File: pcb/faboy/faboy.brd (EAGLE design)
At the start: 85.1 x 54 mm, 58 parts, among them U1 MAX1595UMAX, U2 MCP73831, Y1 16MHZ

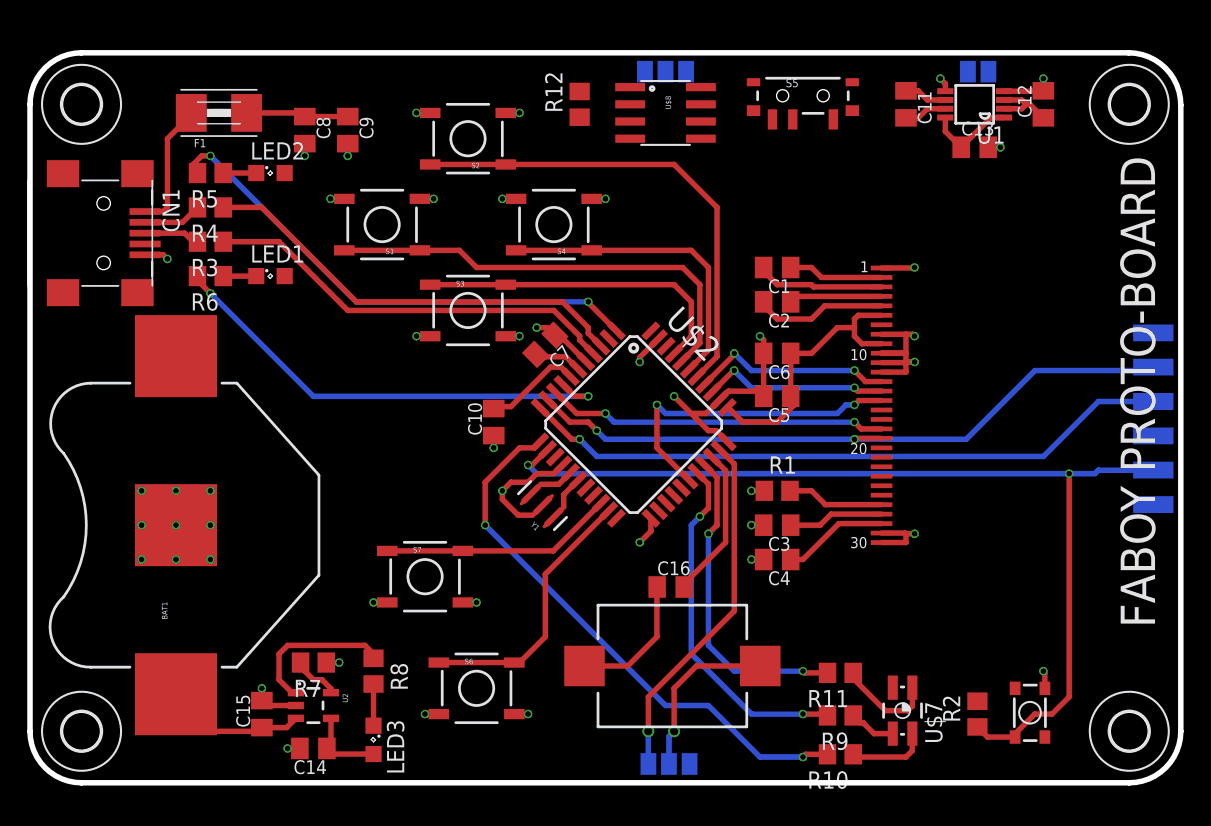
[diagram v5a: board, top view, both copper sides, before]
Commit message: pcb > end of routing
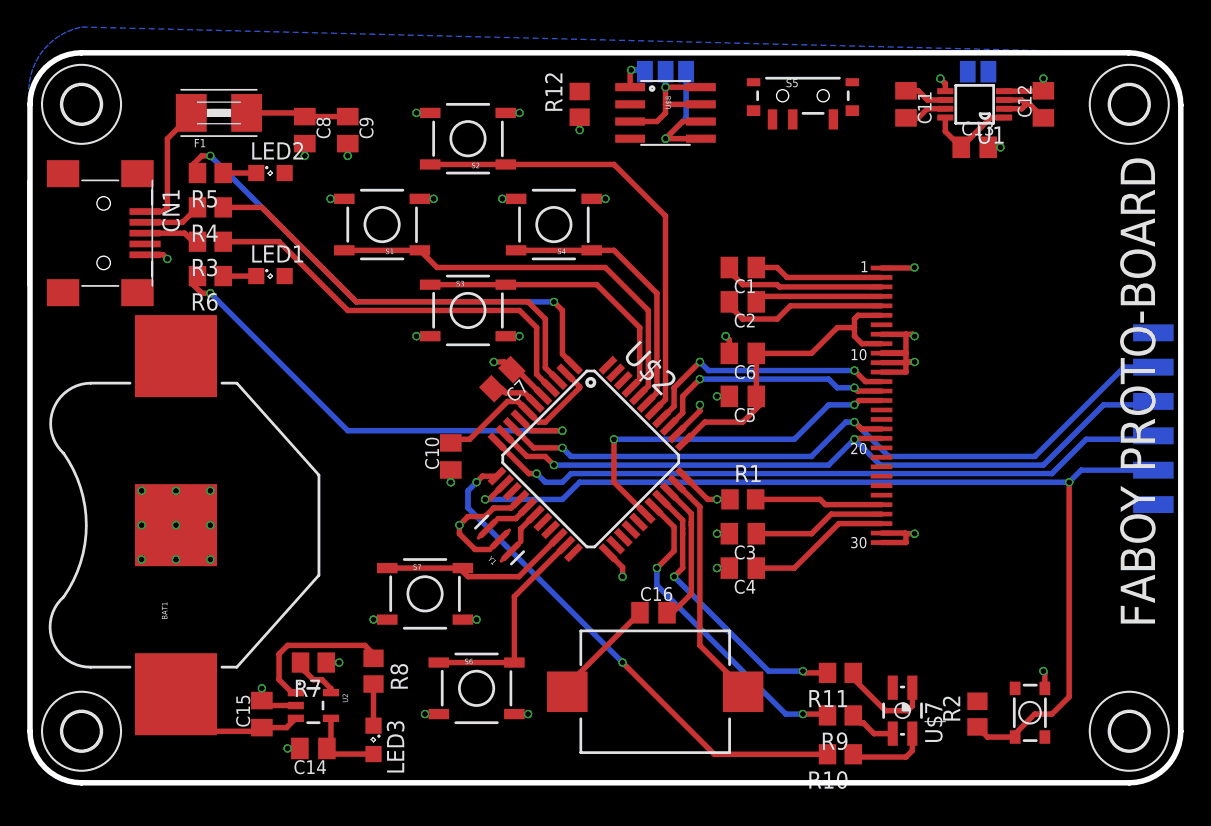
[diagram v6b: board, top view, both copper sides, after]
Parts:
- removed SJ2: (no value), jumper:SJ_2
- SJ1: value (none) -> direct power
- SJ3: value (none) -> direct path
- U$5: value (none) -> gnd
- moved C10 4.07 mm to (31.1, 24.1)
- moved C7 4.07 mm to (34.9, 29.8)
- moved Y1 4.07 mm to (34.7, 18.0)
- moved U$2 4.07 mm to (41.5, 23.9)
- moved C3 2.62 mm to (52.7, 18.4)
- moved C4 2.62 mm to (52.7, 15.9)
- moved R1 2.62 mm to (52.7, 21.0)
- moved C1 2.54 mm to (52.7, 38.1)
- moved C2 2.54 mm to (52.7, 35.6)
- moved C5 2.54 mm to (52.7, 28.6)
- moved C6 2.54 mm to (52.7, 31.8)
- moved C16 2.29 mm to (46.1, 12.6)
- moved SG1 2.29 mm to (46.2, 6.73)
- moved S7 1.27 mm to (29.2, 14.0)
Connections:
- removed net N$27: SJ2.3, U$2.32
- net GND: no longer SJ2.1
- net MISO: now also J2.3; no longer J2.4
- net MOSI: now also J2.4; no longer J2.5
- net N$26: now also U$2.32; no longer SJ2.2
- net SCLK: now also J2.5; no longer J2.3
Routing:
- net SCLK: track 25.3 -> 55.4 mm
- net N$27: track 26.3 -> 0.00 mm, vias 1 -> 0
- net VBAT: track 10.5 -> 21.9 mm, vias 0 -> 1
- net N$28: track 0.00 -> 11.2 mm, vias 0 -> 1
- net GND: track 87.0 -> 78.1 mm, vias 45 -> 46
- net UVCC: track 16.8 -> 23.5 mm
- net N$26: track 12.8 -> 17.4 mm, vias 1 -> 0
- net CS: track 15.0 -> 19.4 mm
- net OLED_RST: track 13.8 -> 18.2 mm
- net B: track 19.9 -> 15.9 mm
- net MOSI: track 50.5 -> 54.5 mm
- net DC: track 23.8 -> 27.5 mm
- net VCC: track 27.7 -> 31.1 mm
- net RST: track 73.5 -> 76.6 mm
- net A: track 17.3 -> 14.3 mm
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- added copper zone on layer 16, net GND

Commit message: pcb > final with silk
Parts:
- moved R12 1.27 mm to (40.6, 48.9)
- turned S2 to 0 degrees
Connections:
- removed net UVCC: C10.2, CN1.VBUS, F1.1, U$2.2, U$2.7
- new net VBUS: CN1.VBUS, F1.1
- net VIN: now also C10.2, U$2.2, U$2.7
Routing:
- net VCC: track 31.1 -> 85.9 mm, vias 0 -> 4
- net VIN: track 15.9 -> 40.5 mm
- net UVCC: track 23.5 -> 0.00 mm
- net N$10: track 5.22 -> 10.1 mm, vias 0 -> 1
- net VBAT: track 21.9 -> 17.3 mm, vias 1 -> 15
- net GND: track 78.1 -> 80.8 mm, vias 46 -> 47
- net LED_RX: track 36.0 -> 38.4 mm
- net LEFT: track 33.8 -> 35.3 mm
- net LED_TX: track 37.5 -> 38.0 mm
- net D-: track 32.2 -> 32.6 mm, vias 0 -> 2
- net D+: vias 0 -> 2
- added copper zone on layer 1, net N$10
- added copper zone on layer 1, net N$28
- added copper zone on layer 1, net VBAT
- added copper zone on layer 16, net VBAT
- added copper zone on layer 1, net VBUS
- added copper zone on layer 1, net VCC
- added copper zone on layer 1, net VIN
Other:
- board text added: "/Users/mayencourtlouis/Documents/projets/faboy/pcb/qrcode_github.bmp"
- board text added: "Mayencourt Louis"
- board text added: "charge"
- board text added: "direct path"
- board text added: "direct power"
- board text added: "embedded systems engineer"
- board text added: "gnd"
- board text added: "louis.mayencourt@gmail.com"
- board text added: "miso"
- board text added: "mosi"
- board text added: "off"
- board text added: "on"
- board text added: "reset"
- board text added: "rst"
- board text added: "rx"
- board text added: "sckl"
- board text added: "tx"
- board text added: "vcc"
- board text removed: "/home/louis/eagle/faboy/pcb/qrcode_github.bmp"
- board text removed: "/home/louis/eagle/faboy/pcb/qrcode_id.bmp"

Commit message: soft > add faboy in core lib
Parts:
- C11: value 1uF -> 0.47uF
- C12, C13: value 1uF -> 2.2uF
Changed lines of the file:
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@@
 <layers>
 <layer number="1" name="Top" color="4" fill="1" visible="yes" active="yes"/>
-<layer number="16" name="Bottom" color="1" fill="1" visible="yes" active="yes"/>
+<layer number="16" name="Bottom" color="1" fill="1" visible="no" active="yes"/>
 <layer number="17" name="Pads" color="2" fill="1" visible="yes" active="yes"/>
 <layer number="18" name="Vias" color="2" fill="1" visible="yes" active="yes"/>
@@
 <layer number="21" name="tPlace" color="7" fill="1" visible="yes" active="yes"/>
 <layer number="22" name="bPlace" color="7" fill="1" visible="yes" active="yes"/>
-<layer number="23" name="tOrigins" color="15" fill="1" visible="no" active="yes"/>
+<layer number="23" name="tOrigins" color="15" fill="1" visible="yes" active="yes"/>
 <layer number="24" name="bOrigins" color="15" fill="1" visible="no" active="yes"/>
-<layer number="25" name="tNames" color="7" fill="1" visible="no" active="yes"/>
+<layer number="25" name="tNames" color="7" fill="1" visible="yes" active="yes"/>
 <layer number="26" name="bNames" color="7" fill="1" visible="no" active="yes"/>
 <layer number="27" name="tValues" color="7" fill="1" visible="no" active="yes"/>
@@
 <layer number="46" name="Milling" color="3" fill="1" visible="no" active="yes"/>
 <layer number="47" name="Measures" color="7" fill="1" visible="no" active="yes"/>
-<layer number="48" name="Document" color="7" fill="1" visible="no" active="yes"/>
+<layer number="48" name="Document" color="7" fill="1" visible="yes" active="yes"/>
 <layer number="49" name="Reference" color="7" fill="1" visible="no" active="yes"/>
 <layer number="50" name="dxf" color="7" fill="1" visible="no" active="no"/>
-<layer number="51" name="tDocu" color="7" fill="1" visible="no" active="yes"/>
+<layer number="51" name="tDocu" color="7" fill="1" visible="yes" active="yes"/>
 <layer number="52" name="bDocu" color="7" fill="1" visible="no" active="yes"/>
 <layer number="53" name="tGND_GNDA" color="7" fill="9" visible="no" active="no"/>
@@
 <element name="U$6" library="holes" package="2,8" value="" x="3.81" y="3.81" rot="R270"/>
 <element name="U1" library="maxim" package="UMAX8" value="MAX1595UMAX" x="69.85" y="50.165" rot="R90"/>
-<element name="C11" library="resistor" package="C0805K" value="1uF" x="64.77" y="50.165" rot="R270"/>
-<element name="C12" library="resistor" package="C0805K" value="1uF" x="74.93" y="50.165" rot="R90"/>
-<element name="C13" library="resistor" package="C0805K" value="1uF" x="69.85" y="46.99"/>
+<element name="C11" library="resistor" package="C0805K" value="0.47uF" x="64.77" y="50.165" rot="R270"/>
+<element name="C12" library="resistor" package="C0805K" value="2.2uF" x="74.93" y="50.165" rot="R90"/>
+<element name="C13" library="resistor" package="C0805K" value="2.2uF" x="69.85" y="46.99"/>
 <element name="J2" library="SparkFun-Connectors" package="1X06-SMD-FEMALE-V2" value="" x="86.487" y="26.924" rot="MR270">
 <attribute name="PROD_ID" value="CONN-09668" x="86.487" y="26.924" size="1.778" layer="28" rot="MR270" display="off"/>
